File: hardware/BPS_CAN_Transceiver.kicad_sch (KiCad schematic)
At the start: 9 parts, among them IC2 TCAN3413DR

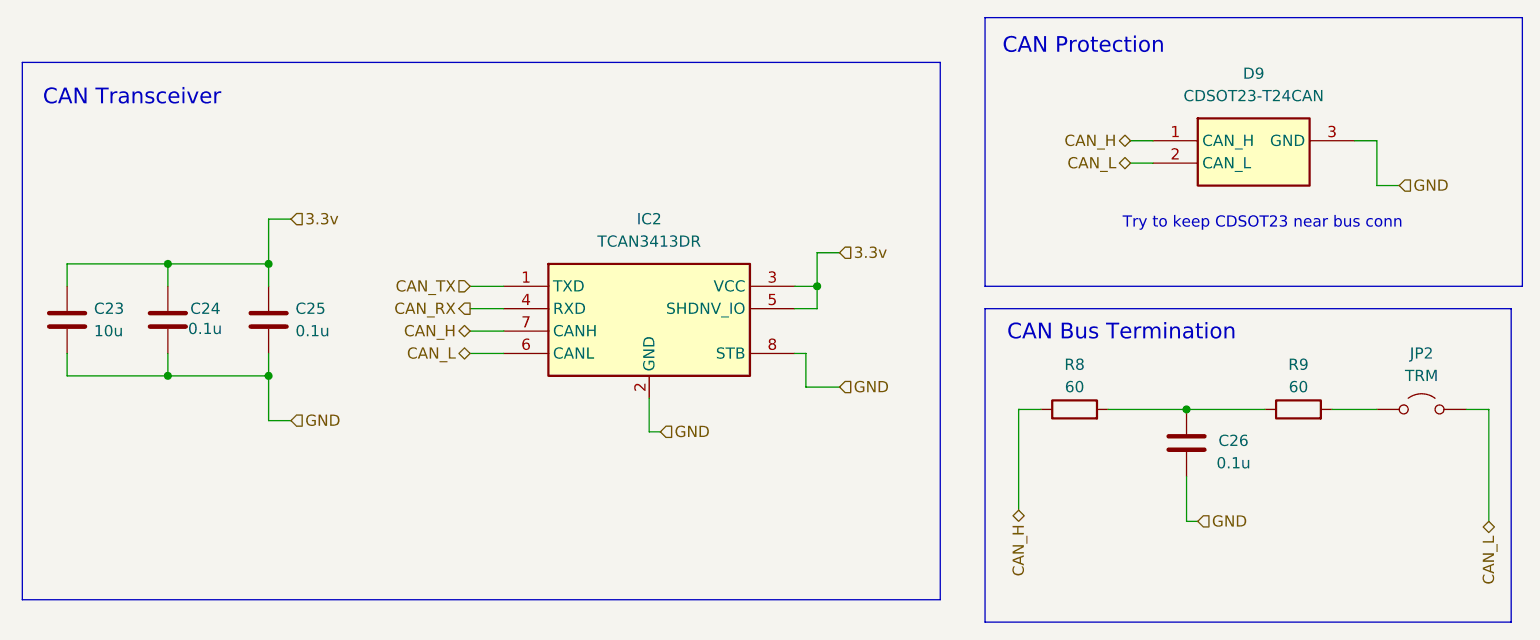
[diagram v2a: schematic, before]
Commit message: finished schematic except for 12v buck boost
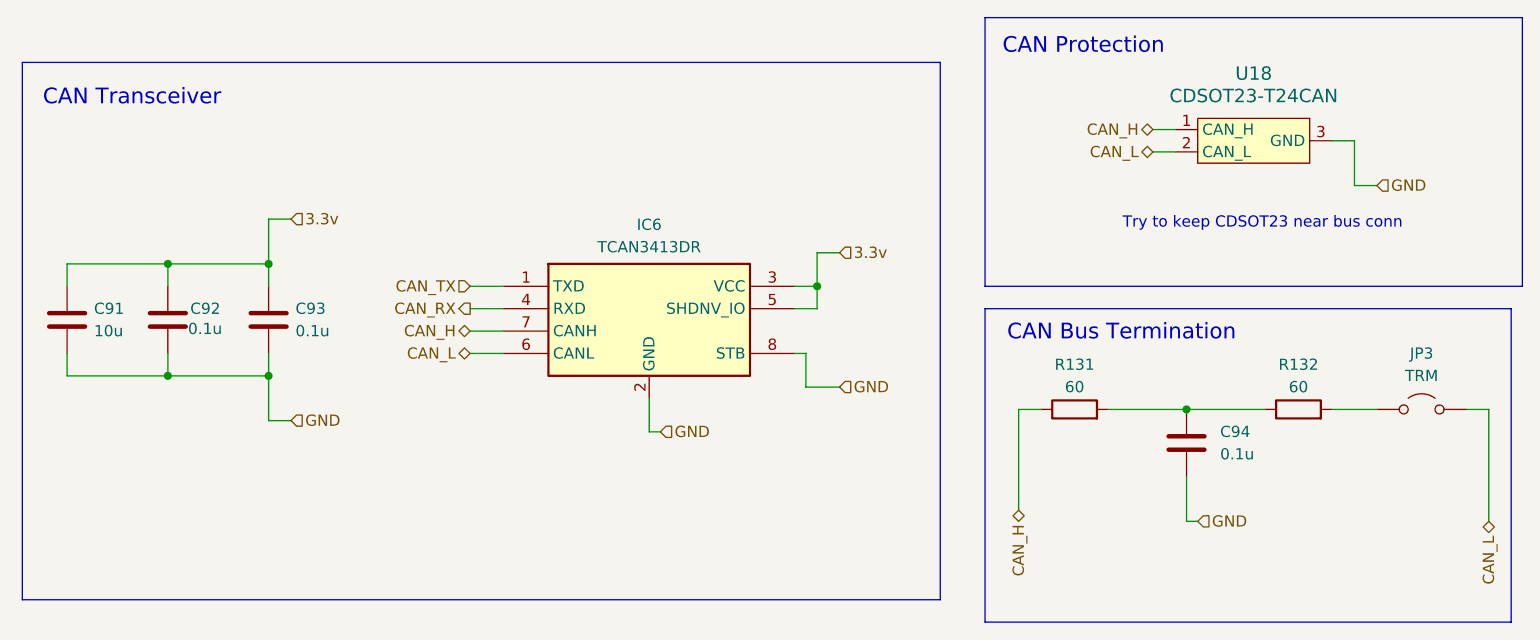
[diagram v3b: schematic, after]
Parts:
- removed C23: 10u, Capacitor_SMD:C_0805_2012Metric_Pad1.18x1.45mm_HandSolder, symbol Device:C
- removed C24, C25: 0.1u, Capacitor_SMD:C_0603_1608Metric_Pad1.08x0.95mm_HandSolder, symbol Device:C
- removed C26: 0.1u, Capacitor_SMD:C_0603_1608Metric_Pad1.08x0.95mm_HandSolder, symbol ECE319K:C
- removed D9: CDSOT23-T24CAN, UTSVT_Passives:CDSOT23-T24CAN, symbol CDSOT23-T24CAN:CDSOT23-T24CAN
- removed IC2: TCAN3413DR, UTSVT_Passives:TCAN3413DR, symbol TCAN3413DR:TCAN3413DR
- removed JP2: TRM, Connector_PinHeader_2.54mm:PinHeader_1x02_P2.54mm_Vertical, symbol Jumper:Jumper_2_Open
- removed R8, R9: 60, Resistor_SMD:R_0603_1608Metric_Pad0.98x0.95mm_HandSolder, symbol Device:R
- added C91: 10u, Capacitor_SMD:C_0805_2012Metric_Pad1.18x1.45mm_HandSolder, symbol Device:C
- added C92, C93: 0.1u, Capacitor_SMD:C_0603_1608Metric_Pad1.08x0.95mm_HandSolder, symbol Device:C
- added C94: 0.1u, symbol Device:C
- added IC6: TCAN3413DR, LHRS_Passives:TCAN3413DR, symbol lhrs_ics:TCAN3413DR
- added JP3: TRM, Connector_PinHeader_2.54mm:PinHeader_1x02_P2.54mm_Vertical, symbol Jumper:Jumper_2_Open
- added R131, R132: 60, Resistor_SMD:R_0603_1608Metric_Pad0.98x0.95mm_HandSolder, symbol Device:R
- added U18: CDSOT23-T24CAN, LHRS_ICs:CDSOT23-T24CAN, symbol lhrs_ics:CDSOT23-T24CAN
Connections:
- net 3.3v: now also C91.1, C92.1, C93.1, IC6.3 (VCC), IC6.5 (SHDNV_IO)
- net CAN_H: now also IC6.7 (CANH), R131.1, U18.1 (CAN_H)
- net CAN_L: now also IC6.6 (CANL), JP3.2 (B), U18.2 (CAN_L)
- net CAN_RX: now also IC6.4 (RXD)
- net CAN_TX: now also IC6.1 (TXD)
- net GND: now also C91.2, C92.2, C93.2, C94.2, IC6.2 (GND), IC6.8 (STB), U18.3 (GND)
- new net: C94.1, R131.2, R132.1
- new net: JP3.1 (A), R132.2

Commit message: added 12V buck boost
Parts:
- C95: renamed from C94; footprint (none) -> Capacitor_SMD:C_0603_1608Metric_Pad1.08x0.95mm_HandSolder
- renumbered C91 to C92, C92 to C93, C93 to C94, R131 to R135, R132 to R136
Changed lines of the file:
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@@
 		(dnp no)
 		(fields_autoplaced yes)
-		(property "Reference" "C94"
+		(property "Reference" "C95"
 			(at 193.04 87.6299 0)
 			(show_name no)
@@
 			)
 		)
-		(property "Footprint" ""
+		(property "Footprint" "Capacitor_SMD:C_0603_1608Metric_Pad1.08x0.95mm_HandSolder"
 			(at 190.1952 92.71 0)
 			(hide yes)
@@
 			(project "PS-BPSLeader"
 				(path "/d4a4ed4f-0983-4aef-b212-0e3284ab3963/5da56964-fa04-4fec-bdfe-c6acfeda5c9a/bbf4edc3-024d-405c-a803-bdefa7ee14fe"
-					(reference "C94")
+					(reference "C95")
 					(unit 1)
 				)
@@
 		(in_pos_files yes)
 		(dnp no)
-		(property "Reference" "R131"
+		(property "Reference" "R135"
 			(at 176.53 80.01 90)
 			(show_name no)
@@
 			(project "PS-BPSLeader"
 				(path "/d4a4ed4f-0983-4aef-b212-0e3284ab3963/5da56964-fa04-4fec-bdfe-c6acfeda5c9a/bbf4edc3-024d-405c-a803-bdefa7ee14fe"
-					(reference "R131")
+					(reference "R135")
 					(unit 1)
 				)
@@
 		(in_pos_files yes)
 		(dnp no)
-		(property "Reference" "C91"
+		(property "Reference" "C92"
 			(at 65.278 73.66 0)
 			(show_name no)
@@
 			(project "PS-BPSLeader"
 				(path "/d4a4ed4f-0983-4aef-b212-0e3284ab3963/5da56964-fa04-4fec-bdfe-c6acfeda5c9a/bbf4edc3-024d-405c-a803-bdefa7ee14fe"
-					(reference "C91")
+					(reference "C92")
 					(unit 1)
 				)
@@
 		(in_pos_files yes)
 		(dnp no)
-		(property "Reference" "C93"
+		(property "Reference" "C94"
 			(at 88.138 73.66 0)
 			(show_name no)
@@
 			(project "PS-BPSLeader"
 				(path "/d4a4ed4f-0983-4aef-b212-0e3284ab3963/5da56964-fa04-4fec-bdfe-c6acfeda5c9a/bbf4edc3-024d-405c-a803-bdefa7ee14fe"
-					(reference "C93")
+					(reference "C94")
 					(unit 1)
 				)
@@
 		(in_pos_files yes)
 		(dnp no)
-		(property "Reference" "R132"
+		(property "Reference" "R136"
 			(at 201.93 80.01 90)
 			(show_name no)
@@
 			(project "PS-BPSLeader"
 				(path "/d4a4ed4f-0983-4aef-b212-0e3284ab3963/5da56964-fa04-4fec-bdfe-c6acfeda5c9a/bbf4edc3-024d-405c-a803-bdefa7ee14fe"
-					(reference "R132")
+					(reference "R136")
 					(unit 1)
 				)
@@
 		(in_pos_files yes)
 		(dnp no)
-		(property "Reference" "C92"
+		(property "Reference" "C93"
 			(at 76.2 73.66 0)
 			(show_name no)
@@
 			(project "PS-BPSLeader"
 				(path "/d4a4ed4f-0983-4aef-b212-0e3284ab3963/5da56964-fa04-4fec-bdfe-c6acfeda5c9a/bbf4edc3-024d-405c-a803-bdefa7ee14fe"
-					(reference "C92")
+					(reference "C93")
 					(unit 1)
 				)
